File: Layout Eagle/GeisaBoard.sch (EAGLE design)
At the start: 20 parts, among them IC1 4052N, IC2 4052N, U1 328P

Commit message: Versão inicial do Layout feita
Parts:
- U$3: device diy-modules:RTC-DS3231-AT24C32 -> Geisa:RTC-DS3231-AT24C32
- renumbered J2 to SAIDA_L0, J3 to SAIDA_L1, J4 to SAIDA_L2, J5 to SAIDA_L3
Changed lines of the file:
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@@
 <part name="GND4" library="SparkFun-PowerSymbols" deviceset="GND" device=""/>
 <part name="SUPPLY10" library="SparkFun-PowerSymbols" deviceset="VCC" device=""/>
-<part name="J2" library="SparkFun-Connectors" deviceset="DB9" device="FEMALE"/>
-<part name="J3" library="SparkFun-Connectors" deviceset="DB9" device="FEMALE"/>
-<part name="J4" library="SparkFun-Connectors" deviceset="DB9" device="FEMALE"/>
-<part name="J5" library="SparkFun-Connectors" deviceset="DB9" device="FEMALE"/>
-<part name="U$3" library="diy-modules" deviceset="RTC-DS3231-AT24C32" device=""/>
+<part name="SAIDA_L0" library="SparkFun-Connectors" deviceset="DB9" device="FEMALE"/>
+<part name="SAIDA_L1" library="SparkFun-Connectors" deviceset="DB9" device="FEMALE"/>
+<part name="SAIDA_L2" library="SparkFun-Connectors" deviceset="DB9" device="FEMALE"/>
+<part name="SAIDA_L3" library="SparkFun-Connectors" deviceset="DB9" device="FEMALE"/>
+<part name="U$3" library="Geisa" deviceset="RTC-DS3231-AT24C32" device=""/>
 <part name="U$4" library="Geisa" deviceset="CARD-MICRO-SD-ADAPTER" device=""/>
 </parts>
@@
 <instance part="GND4" gate="1" x="22.86" y="-50.8"/>
 <instance part="SUPPLY10" gate="G$1" x="22.86" y="-38.1"/>
-<instance part="J2" gate="G$1" x="137.16" y="91.44"/>
-<instance part="J3" gate="G$1" x="137.16" y="53.34"/>
-<instance part="J4" gate="G$1" x="137.16" y="10.16"/>
-<instance part="J5" gate="G$1" x="137.16" y="-30.48"/>
+<instance part="SAIDA_L0" gate="G$1" x="137.16" y="91.44"/>
+<instance part="SAIDA_L1" gate="G$1" x="137.16" y="53.34"/>
+<instance part="SAIDA_L2" gate="G$1" x="137.16" y="10.16"/>
+<instance part="SAIDA_L3" gate="G$1" x="137.16" y="-30.48"/>
 <instance part="U$3" gate="G$1" x="45.72" y="66.04"/>
 <instance part="U$4" gate="G$1" x="-58.42" y="-58.42"/>
@@
 <pinref part="GND6" gate="1" pin="GND"/>
 <wire x1="149.86" y1="86.36" x2="149.86" y2="83.82" width="0.1524" layer="91"/>
-<pinref part="J2" gate="G$1" pin="9"/>
+<pinref part="SAIDA_L0" gate="G$1" pin="9"/>
 </segment>
 <segment>
@@
 <pinref part="GND7" gate="1" pin="GND"/>
 <wire x1="149.86" y1="45.72" x2="149.86" y2="48.26" width="0.1524" layer="91"/>
-<pinref part="J3" gate="G$1" pin="9"/>
+<pinref part="SAIDA_L1" gate="G$1" pin="9"/>
 </segment>
 <segment>
@@
 <pinref part="GND8" gate="1" pin="GND"/>
 <wire x1="149.86" y1="2.54" x2="149.86" y2="5.08" width="0.1524" layer="91"/>
-<pinref part="J4" gate="G$1" pin="9"/>
+<pinref part="SAIDA_L2" gate="G$1" pin="9"/>
 </segment>
 <segment>
@@
 <pinref part="GND9" gate="1" pin="GND"/>
 <wire x1="149.86" y1="-38.1" x2="149.86" y2="-35.56" width="0.1524" layer="91"/>
-<pinref part="J5" gate="G$1" pin="9"/>
+<pinref part="SAIDA_L3" gate="G$1" pin="9"/>
 </segment>
 <segment>
@@
 <wire x1="124.46" y1="-33.02" x2="129.54" y2="-33.02" width="0.1524" layer="91"/>
 <label x="119.38" y="-33.02" size="1.778" layer="95"/>
-<pinref part="J5" gate="G$1" pin="4"/>
+<pinref part="SAIDA_L3" gate="G$1" pin="4"/>
 </segment>
 </net>
@@
 <wire x1="129.54" y1="50.8" x2="124.46" y2="50.8" width="0.1524" layer="91"/>
 <label x="119.38" y="50.8" size="1.778" layer="95"/>
-<pinref part="J3" gate="G$1" pin="4"/>
+<pinref part="SAIDA_L1" gate="G$1" pin="4"/>
 </segment>
 </net>
@@
 <wire x1="124.46" y1="-30.48" x2="129.54" y2="-30.48" width="0.1524" layer="91"/>
 <label x="121.92" y="-30.48" size="1.778" layer="95"/>
-<pinref part="J5" gate="G$1" pin="3"/>
+<pinref part="SAIDA_L3" gate="G$1" pin="3"/>
 </segment>
 </net>
@@
 <wire x1="124.46" y1="10.16" x2="129.54" y2="10.16" width="0.1524" layer="91"/>
 <label x="121.92" y="10.16" size="1.778" layer="95"/>
-<pinref part="J4" gate="G$1" pin="3"/>
+<pinref part="SAIDA_L2" gate="G$1" pin="3"/>
 </segment>
 </net>
@@
 <wire x1="129.54" y1="53.34" x2="124.46" y2="53.34" width="0.1524" layer="91"/>
 <label x="121.92" y="53.34" size="1.778" layer="95"/>
-<pinref part="J3" gate="G$1" pin="3"/>
+<pinref part="SAIDA_L1" gate="G$1" pin="3"/>
 </segment>
 </net>
@@
 <wire x1="129.54" y1="91.44" x2="124.46" y2="91.44" width="0.1524" layer="91"/>
 <label x="121.92" y="91.44" size="1.778" layer="95"/>
-<pinref part="J2" gate="G$1" pin="3"/>
+<pinref part="SAIDA_L0" gate="G$1" pin="3"/>
 </segment>
 </net>
@@
 <pinref part="SUPPLY6" gate="G$1" pin="VCC"/>
 <wire x1="124.46" y1="-25.4" x2="124.46" y2="-22.86" width="0.1524" layer="91"/>
-<pinref part="J5" gate="G$1" pin="1"/>
+<pinref part="SAIDA_L3" gate="G$1" pin="1"/>
 </segment>
 <segment>
@@
 <pinref part="SUPPLY7" gate="G$1" pin="VCC"/>
 <wire x1="124.46" y1="17.78" x2="124.46" y2="15.24" width="0.1524" layer="91"/>
-<pinref part="J4" gate="G$1" pin="1"/>
+<pinref part="SAIDA_L2" gate="G$1" pin="1"/>
 </segment>
 <segment>
@@
 <pinref part="SUPPLY8" gate="G$1" pin="VCC"/>
 <wire x1="124.46" y1="60.96" x2="124.46" y2="58.42" width="0.1524" layer="91"/>
-<pinref part="J3" gate="G$1" pin="1"/>
+<pinref part="SAIDA_L1" gate="G$1" pin="1"/>
 </segment>
 <segment>
@@
 <pinref part="SUPPLY9" gate="G$1" pin="VCC"/>
 <wire x1="124.46" y1="99.06" x2="124.46" y2="96.52" width="0.1524" layer="91"/>
-<pinref part="J2" gate="G$1" pin="1"/>
+<pinref part="SAIDA_L0" gate="G$1" pin="1"/>
 </segment>
 <segment>
@@
 <wire x1="129.54" y1="88.9" x2="124.46" y2="88.9" width="0.1524" layer="91"/>
 <label x="119.38" y="88.9" size="1.778" layer="95"/>
-<pinref part="J2" gate="G$1" pin="4"/>
+<pinref part="SAIDA_L0" gate="G$1" pin="4"/>
 </segment>
 </net>
@@
 <wire x1="124.46" y1="7.62" x2="129.54" y2="7.62" width="0.1524" layer="91"/>
 <label x="119.38" y="7.62" size="1.778" layer="95"/>
-<pinref part="J4" gate="G$1" pin="4"/>
+<pinref part="SAIDA_L2" gate="G$1" pin="4"/>
 </segment>
 <segment>
@@
 <wire x1="129.54" y1="93.98" x2="124.46" y2="93.98" width="0.1524" layer="91"/>
 <label x="121.92" y="93.98" size="1.778" layer="95"/>
-<pinref part="J2" gate="G$1" pin="2"/>
+<pinref part="SAIDA_L0" gate="G$1" pin="2"/>
 </segment>
 </net>
@@
 <wire x1="129.54" y1="55.88" x2="124.46" y2="55.88" width="0.1524" layer="91"/>
 <label x="121.92" y="55.88" size="1.778" layer="95"/>
-<pinref part="J3" gate="G$1" pin="2"/>
+<pinref part="SAIDA_L1" gate="G$1" pin="2"/>
 </segment>
 </net>
@@
 <wire x1="129.54" y1="12.7" x2="124.46" y2="12.7" width="0.1524" layer="91"/>
 <label x="121.92" y="12.7" size="1.778" layer="95"/>
-<pinref part="J4" gate="G$1" pin="2"/>
+<pinref part="SAIDA_L2" gate="G$1" pin="2"/>
 </segment>
 </net>
@@
 <wire x1="129.54" y1="-27.94" x2="124.46" y2="-27.94" width="0.1524" layer="91"/>
 <label x="121.92" y="-27.94" size="1.778" layer="95"/>
-<pinref part="J5" gate="G$1" pin="2"/>
+<pinref part="SAIDA_L3" gate="G$1" pin="2"/>
 </segment>
 </net>
@@
 <wire x1="144.78" y1="88.9" x2="149.86" y2="88.9" width="0.1524" layer="91"/>
 <label x="154.94" y="88.9" size="1.778" layer="95" rot="MR0"/>
-<pinref part="J2" gate="G$1" pin="8"/>
+<pinref part="SAIDA_L0" gate="G$1" pin="8"/>
 </segment>
 <segment>
 <wire x1="144.78" y1="50.8" x2="149.86" y2="50.8" width="0.1524" layer="91"/>
 <label x="154.94" y="50.8" size="1.778" layer="95" rot="MR0"/>
-<pinref part="J3" gate="G$1" pin="8"/>
+<pinref part="SAIDA_L1" gate="G$1" pin="8"/>
 </segment>
 <segment>
 <wire x1="149.86" y1="7.62" x2="144.78" y2="7.62" width="0.1524" layer="91"/>
 <label x="154.94" y="7.62" size="1.778" layer="95" rot="MR0"/>
-<pinref part="J4" gate="G$1" pin="8"/>
+<pinref part="SAIDA_L2" gate="G$1" pin="8"/>
 </segment>
 <segment>
 <wire x1="149.86" y1="-33.02" x2="144.78" y2="-33.02" width="0.1524" layer="91"/>
 <label x="154.94" y="-33.02" size="1.778" layer="95" rot="MR0"/>
-<pinref part="J5" gate="G$1" pin="8"/>
+<pinref part="SAIDA_L3" gate="G$1" pin="8"/>
 </segment>
 </net>
@@
 <wire x1="144.78" y1="93.98" x2="149.86" y2="93.98" width="0.1524" layer="91"/>
 <label x="154.94" y="93.98" size="1.778" layer="95" rot="MR0"/>
-<pinref part="J2" gate="G$1" pin="6"/>
+<pinref part="SAIDA_L0" gate="G$1" pin="6"/>
 </segment>
 <segment>
 <wire x1="144.78" y1="55.88" x2="149.86" y2="55.88" width="0.1524" layer="91"/>
 <label x="154.94" y="55.88" size="1.778" layer="95" rot="MR0"/>
-<pinref part="J3" gate="G$1" pin="6"/>
+<pinref part="SAIDA_L1" gate="G$1" pin="6"/>
 </segment>
 <segment>
 <wire x1="149.86" y1="12.7" x2="144.78" y2="12.7" width="0.1524" layer="91"/>
 <label x="154.94" y="12.7" size="1.778" layer="95" rot="MR0"/>
-<pinref part="J4" gate="G$1" pin="6"/>
+<pinref part="SAIDA_L2" gate="G$1" pin="6"/>
 </segment>
 <segment>
 <wire x1="149.86" y1="-27.94" x2="144.78" y2="-27.94" width="0.1524" layer="91"/>
 <label x="154.94" y="-27.94" size="1.778" layer="95" rot="MR0"/>
-<pinref part="J5" gate="G$1" pin="6"/>
+<pinref part="SAIDA_L3" gate="G$1" pin="6"/>
 </segment>
 </net>
@@
 <wire x1="144.78" y1="91.44" x2="149.86" y2="91.44" width="0.1524" layer="91"/>
 <label x="154.94" y="91.44" size="1.778" layer="95" rot="MR0"/>
-<pinref part="J2" gate="G$1" pin="7"/>
+<pinref part="SAIDA_L0" gate="G$1" pin="7"/>
 </segment>
 <segment>
 <wire x1="144.78" y1="53.34" x2="149.86" y2="53.34" width="0.1524" layer="91"/>
 <label x="154.94" y="53.34" size="1.778" layer="95" rot="MR0"/>
-<pinref part="J3" gate="G$1" pin="7"/>
+<pinref part="SAIDA_L1" gate="G$1" pin="7"/>
 </segment>
 <segment>
 <wire x1="149.86" y1="10.16" x2="144.78" y2="10.16" width="0.1524" layer="91"/>
 <label x="154.94" y="10.16" size="1.778" layer="95" rot="MR0"/>
-<pinref part="J4" gate="G$1" pin="7"/>
+<pinref part="SAIDA_L2" gate="G$1" pin="7"/>
 </segment>
 <segment>
 <wire x1="149.86" y1="-30.48" x2="144.78" y2="-30.48" width="0.1524" layer="91"/>
 <label x="154.94" y="-30.48" size="1.778" layer="95" rot="MR0"/>
-<pinref part="J5" gate="G$1" pin="7"/>
-</segment>
-</net>
+<pinref part="SAIDA_L3" gate="G$1" pin="7"/>
+</segment>
+</net>

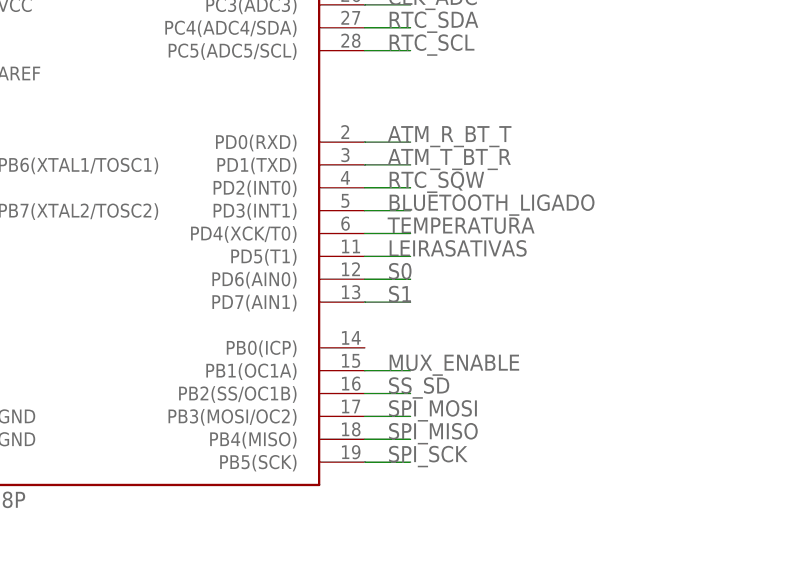
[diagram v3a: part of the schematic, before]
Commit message: Layout com correção inicial do Padrão
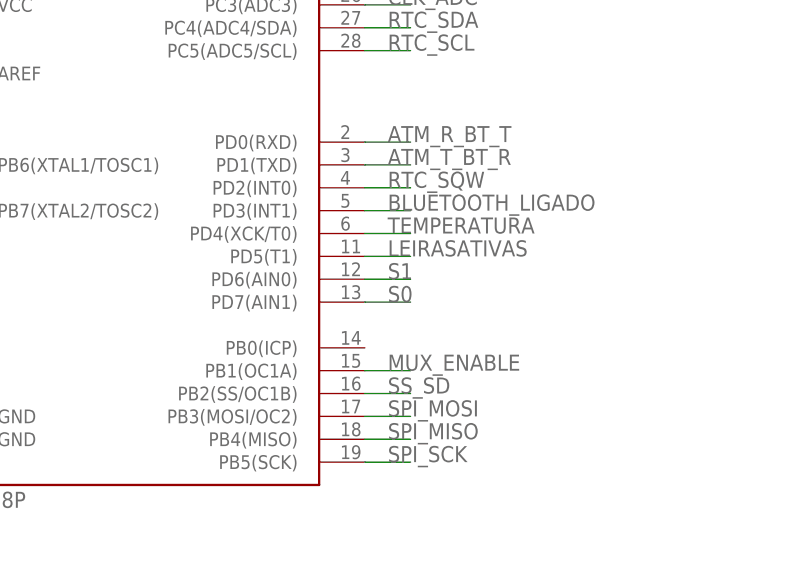
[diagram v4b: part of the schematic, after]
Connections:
- net S0: now also U1.PD7(AIN1); no longer U1.PD6(AIN0)
- net S1: now also U1.PD6(AIN0); no longer U1.PD7(AIN1)
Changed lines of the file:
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@@
 <?xml version="1.0" encoding="utf-8"?>
 <!DOCTYPE eagle SYSTEM "eagle.dtd">
-<eagle version="8.3.2">
+<eagle version="8.7.0">
 <drawing>
 <settings>
@@
 <net name="S0" class="0">
 <segment>
+<wire x1="50.8" y1="12.7" x2="55.88" y2="12.7" width="0.1524" layer="91"/>
+<label x="53.34" y="12.7" size="1.778" layer="95"/>
+<pinref part="IC1" gate="A" pin="A"/>
+</segment>
+<segment>
+<wire x1="55.88" y1="-43.18" x2="50.8" y2="-43.18" width="0.1524" layer="91"/>
+<label x="53.34" y="-43.18" size="1.778" layer="95"/>
+<pinref part="IC2" gate="A" pin="A"/>
+</segment>
+<segment>
+<pinref part="U1" gate="G$1" pin="PD7(AIN1)"/>
+<wire x1="-43.18" y1="7.62" x2="-38.1" y2="7.62" width="0.1524" layer="91"/>
+<label x="-40.64" y="7.62" size="1.778" layer="95"/>
+</segment>
+</net>
+<net name="S1" class="0">
+<segment>
+<wire x1="50.8" y1="10.16" x2="55.88" y2="10.16" width="0.1524" layer="91"/>
+<label x="53.34" y="10.16" size="1.778" layer="95"/>
+<pinref part="IC1" gate="A" pin="B"/>
+</segment>
+<segment>
+<wire x1="55.88" y1="-45.72" x2="50.8" y2="-45.72" width="0.1524" layer="91"/>
+<label x="53.34" y="-45.72" size="1.778" layer="95"/>
+<pinref part="IC2" gate="A" pin="B"/>
+</segment>
+<segment>
 <pinref part="U1" gate="G$1" pin="PD6(AIN0)"/>
 <wire x1="-43.18" y1="10.16" x2="-38.1" y2="10.16" width="0.1524" layer="91"/>
 <label x="-40.64" y="10.16" size="1.778" layer="95"/>
 </segment>
-<segment>
-<wire x1="50.8" y1="12.7" x2="55.88" y2="12.7" width="0.1524" layer="91"/>
-<label x="53.34" y="12.7" size="1.778" layer="95"/>
-<pinref part="IC1" gate="A" pin="A"/>
-</segment>
-<segment>
-<wire x1="55.88" y1="-43.18" x2="50.8" y2="-43.18" width="0.1524" layer="91"/>
-<label x="53.34" y="-43.18" size="1.778" layer="95"/>
-<pinref part="IC2" gate="A" pin="A"/>
-</segment>
-</net>
-<net name="S1" class="0">
-<segment>
-<pinref part="U1" gate="G$1" pin="PD7(AIN1)"/>
-<wire x1="-43.18" y1="7.62" x2="-38.1" y2="7.62" width="0.1524" layer="91"/>
-<label x="-40.64" y="7.62" size="1.778" layer="95"/>
-</segment>
-<segment>
-<wire x1="50.8" y1="10.16" x2="55.88" y2="10.16" width="0.1524" layer="91"/>
-<label x="53.34" y="10.16" size="1.778" layer="95"/>
-<pinref part="IC1" gate="A" pin="B"/>
-</segment>
-<segment>
-<wire x1="55.88" y1="-45.72" x2="50.8" y2="-45.72" width="0.1524" layer="91"/>
-<label x="53.34" y="-45.72" size="1.778" layer="95"/>
-<pinref part="IC2" gate="A" pin="B"/>
-</segment>
-</net>
+</net>
